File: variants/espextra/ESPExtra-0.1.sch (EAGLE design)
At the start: 15 parts, among them U1 ESP12E_DEVKIT, U2 MCP23S17SP, U3 MCP23S17SP, U4 MCP3008

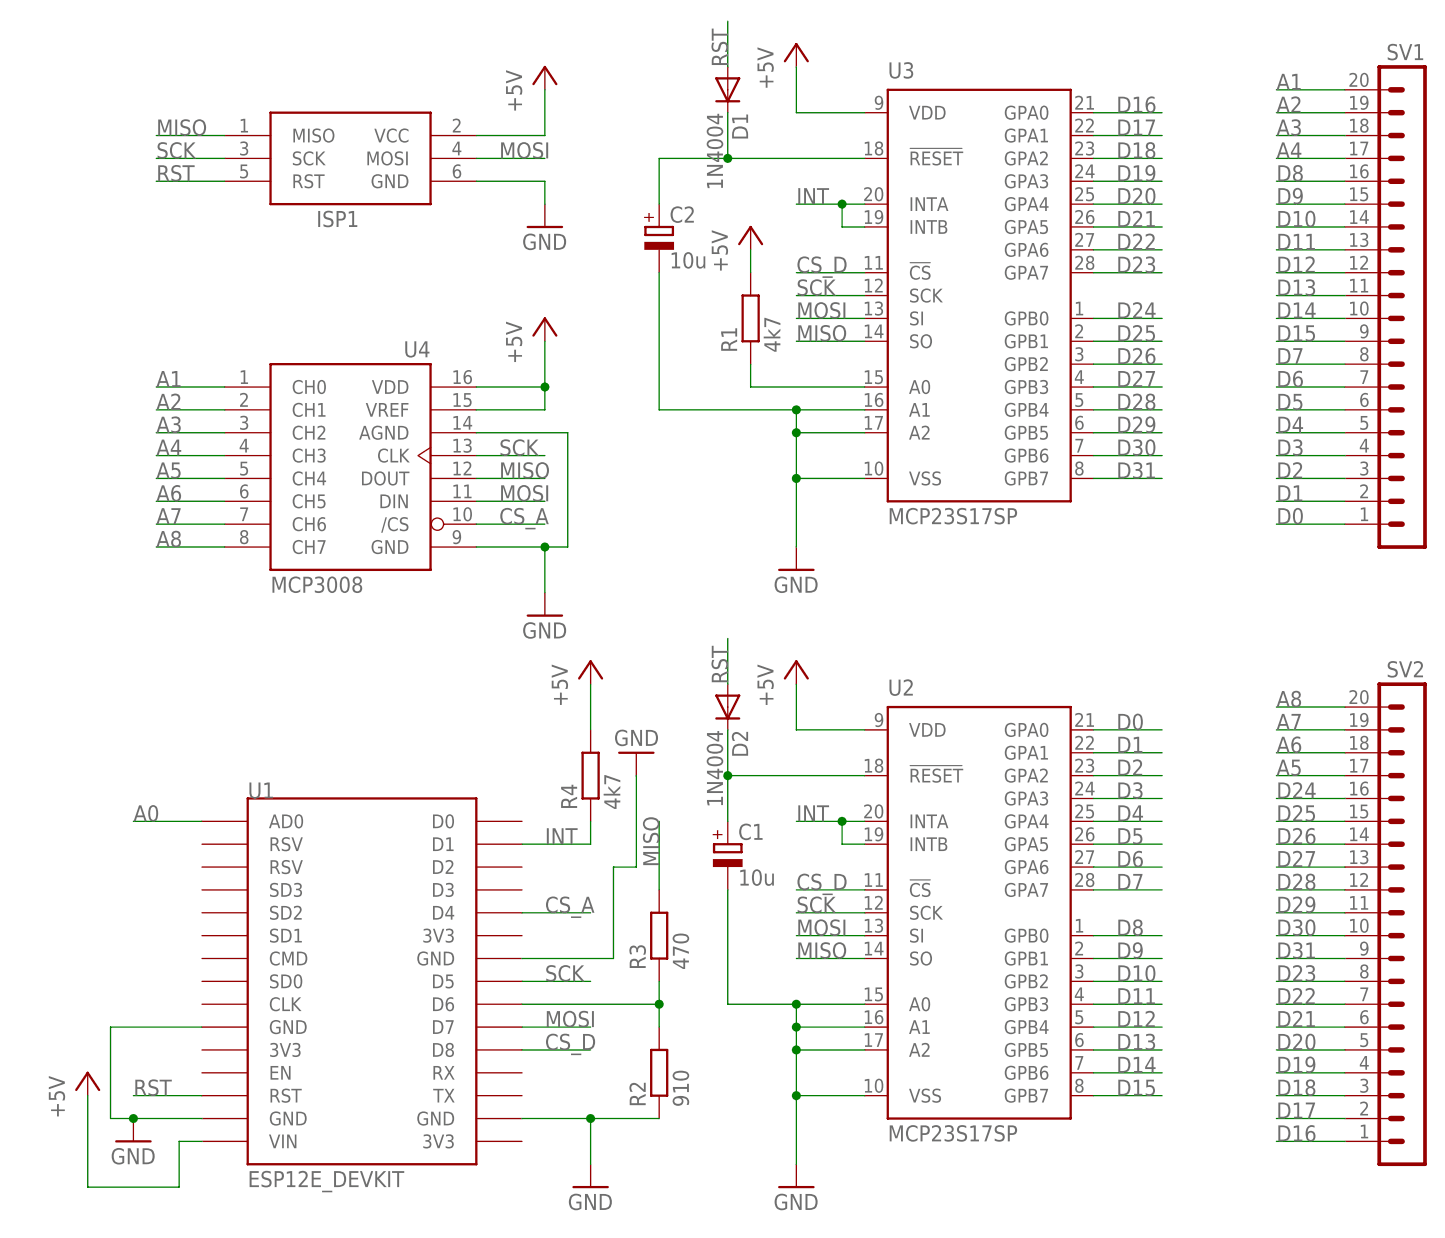
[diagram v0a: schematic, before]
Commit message: Previous commit failed to update board files
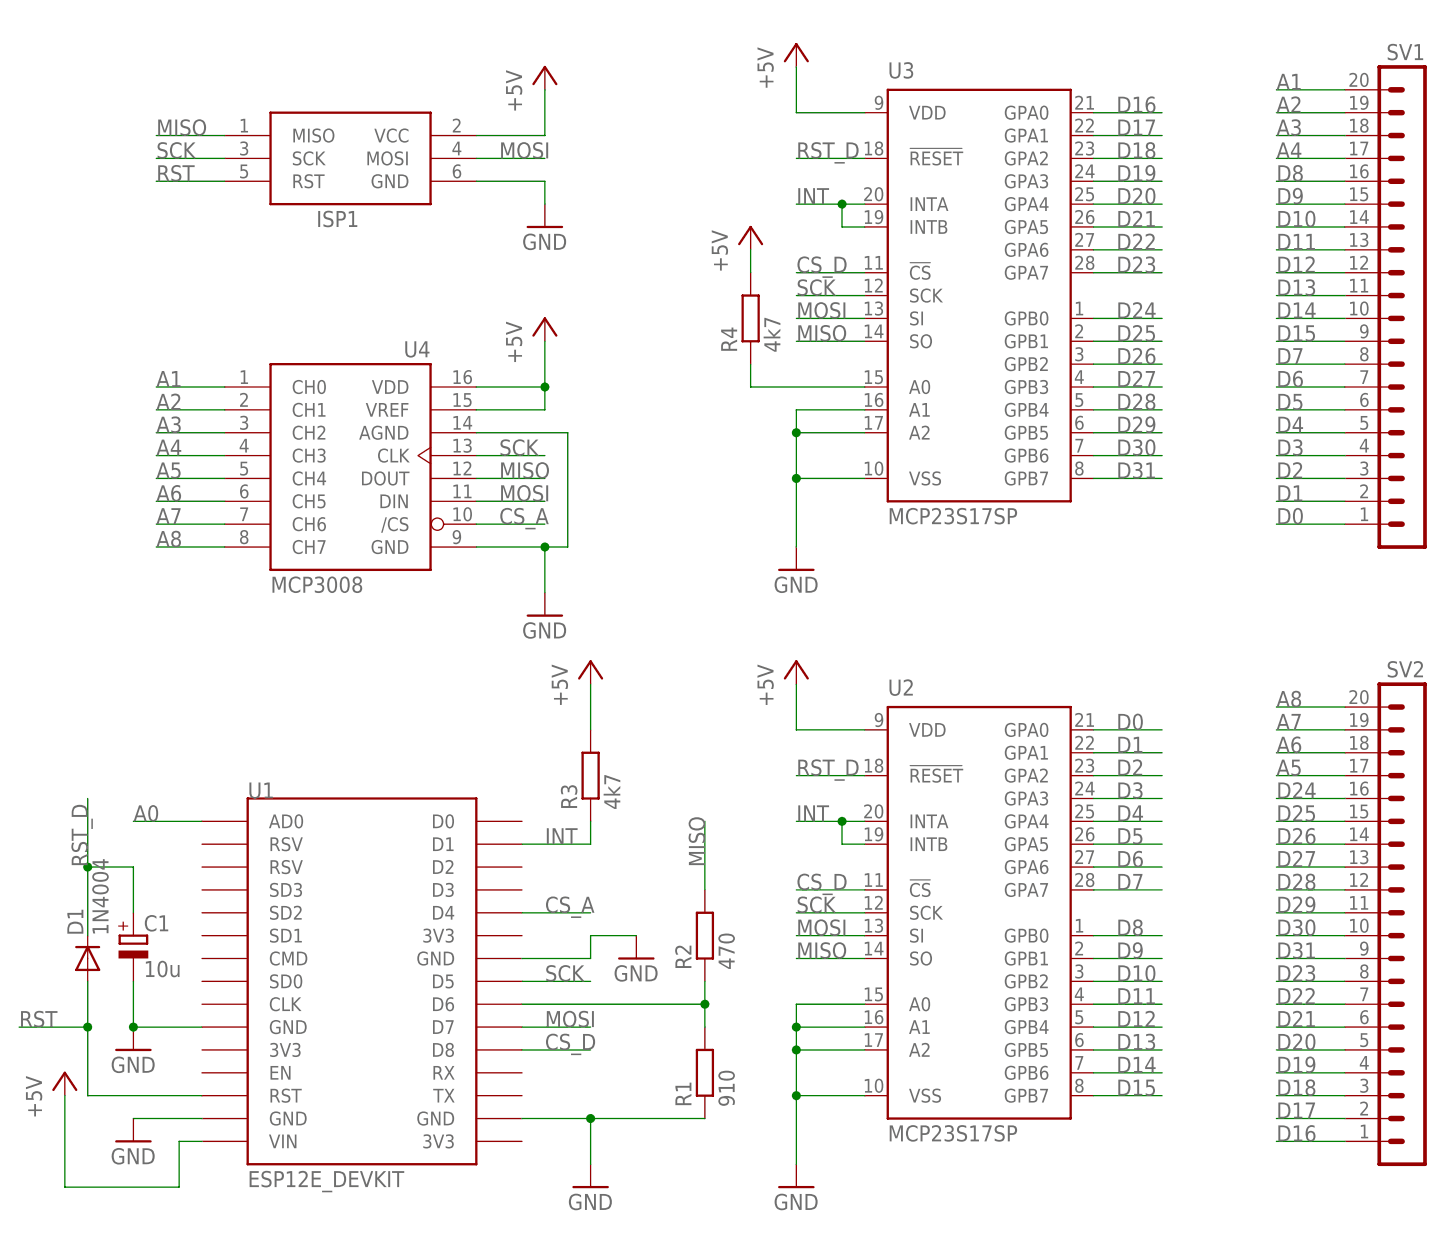
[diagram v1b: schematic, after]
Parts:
- removed C2: 10u, resistor:CPOL-EUE2.5-5
- removed D2: 1N4004, diode:1N4004
- R1: value 4k7 -> 910
- R2: value 910 -> 470
- R3: value 470 -> 4k7
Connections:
- removed net N$3: C2.+, D1.C, U3.!RESET
- removed net N$30: C1.+, D2.C, U2.!RESET
- new net RST_D: C1.+, D1.C, U2.!RESET, U3.!RESET
- net +5V: now also R3.2; no longer R1.2
- net GND: now also R1.1; no longer C2.-, R2.1
- net INT: now also R3.1; no longer R4.1
- net MISO: now also R2.2; no longer R3.2
- net N$11: now also R1.2, R2.1; no longer R2.2, R3.1
- net N$25: now also R4.1; no longer R1.1
- net RST: no longer D2.A
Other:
- moved on the sheet: C1, D1, R1, R2, R3, R4

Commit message: Resistor removed, internal pullup is used for interrupt pin. Also, before SPI transactions, set the appropriate SPI settings, just to be sure.
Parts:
- removed R3: 4k7, resistor:R-EU_0204/5
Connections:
- net +5V: no longer R3.2
- net INT: no longer R3.1
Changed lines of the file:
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@@
 <part name="R2" library="resistor" deviceset="R-EU_" device="0204/5" value="470"/>
 <part name="C1" library="resistor" deviceset="CPOL-EU" device="E2.5-5" value="10u"/>
-<part name="P+7" library="supply1" deviceset="+5V" device=""/>
-<part name="R3" library="resistor" deviceset="R-EU_" device="0204/5" value="4k7"/>
 <part name="GND5" library="supply1" deviceset="GND" device=""/>
 <part name="GND8" library="supply1" deviceset="GND" device=""/>
@@
 <instance part="R2" gate="G$1" x="53.34" y="22.86" rot="R90"/>
 <instance part="C1" gate="G$1" x="-10.16" y="22.86"/>
-<instance part="P+7" gate="1" x="40.64" y="53.34"/>
-<instance part="R3" gate="G$1" x="40.64" y="40.64" rot="R90"/>
 <instance part="GND5" gate="1" x="-10.16" y="10.16"/>
 <instance part="GND8" gate="1" x="45.72" y="20.32"/>
@@
 <wire x1="40.64" y1="33.02" x2="33.02" y2="33.02" width="0.1524" layer="91"/>
 <label x="35.56" y="33.02" size="1.778" layer="95"/>
-<pinref part="R3" gate="G$1" pin="1"/>
-<wire x1="40.64" y1="33.02" x2="40.64" y2="35.56" width="0.1524" layer="91"/>
 </segment>
 </net>
@@
 <wire x1="-17.78" y1="-5.08" x2="-17.78" y2="5.08" width="0.1524" layer="91"/>
 </segment>
-<segment>
-<pinref part="R3" gate="G$1" pin="2"/>
-<pinref part="P+7" gate="1" pin="+5V"/>
-<wire x1="40.64" y1="45.72" x2="40.64" y2="50.8" width="0.1524" layer="91"/>
-</segment>
-</net>
+</net>
